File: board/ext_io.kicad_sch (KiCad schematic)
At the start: 34 parts, among them J13 AIN, J14 CAN_1, J15 DIO1, J16 DIO0, J17 CAN_2, SW10 Term, SW9 Term, U12 25LCxxx, U13 MCP2515-xP, U14 MCP3204, U15 MCP2562-E-P, U16 MCP2515-xP, U17 MCP23S17_SP, U18 MCP2562-E-P, Y2 16MHz, Y3 16MHz

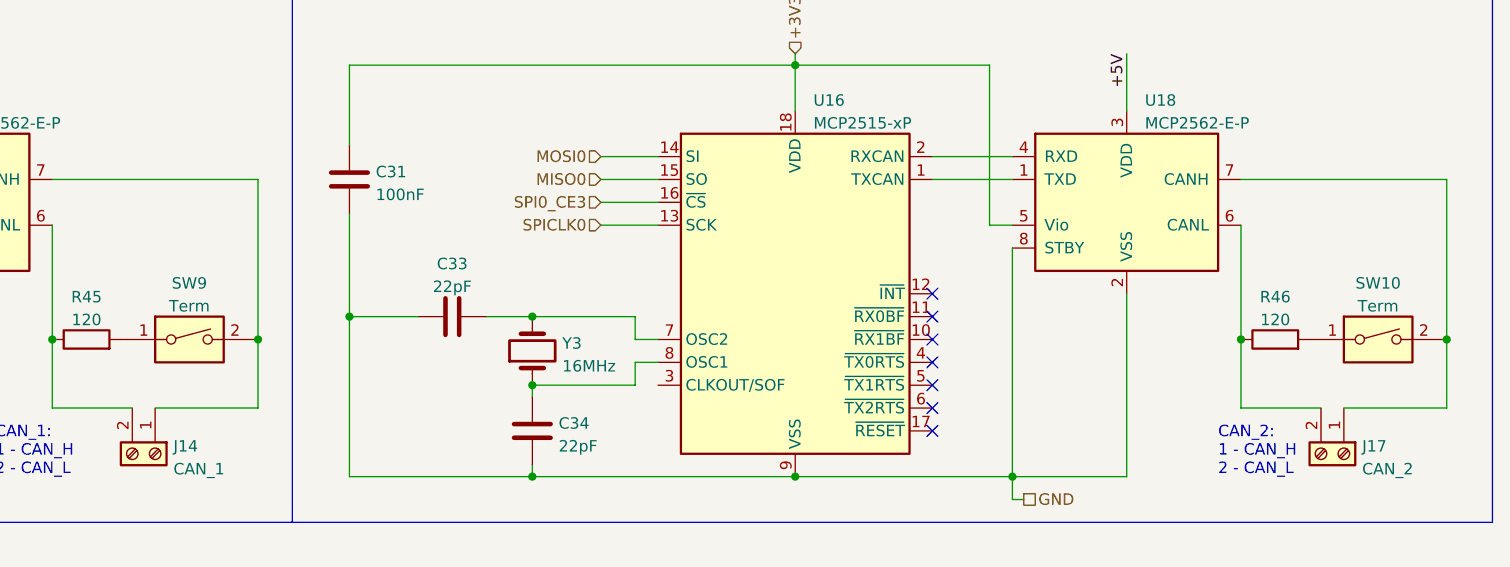
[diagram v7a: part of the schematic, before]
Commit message: Modularize board.
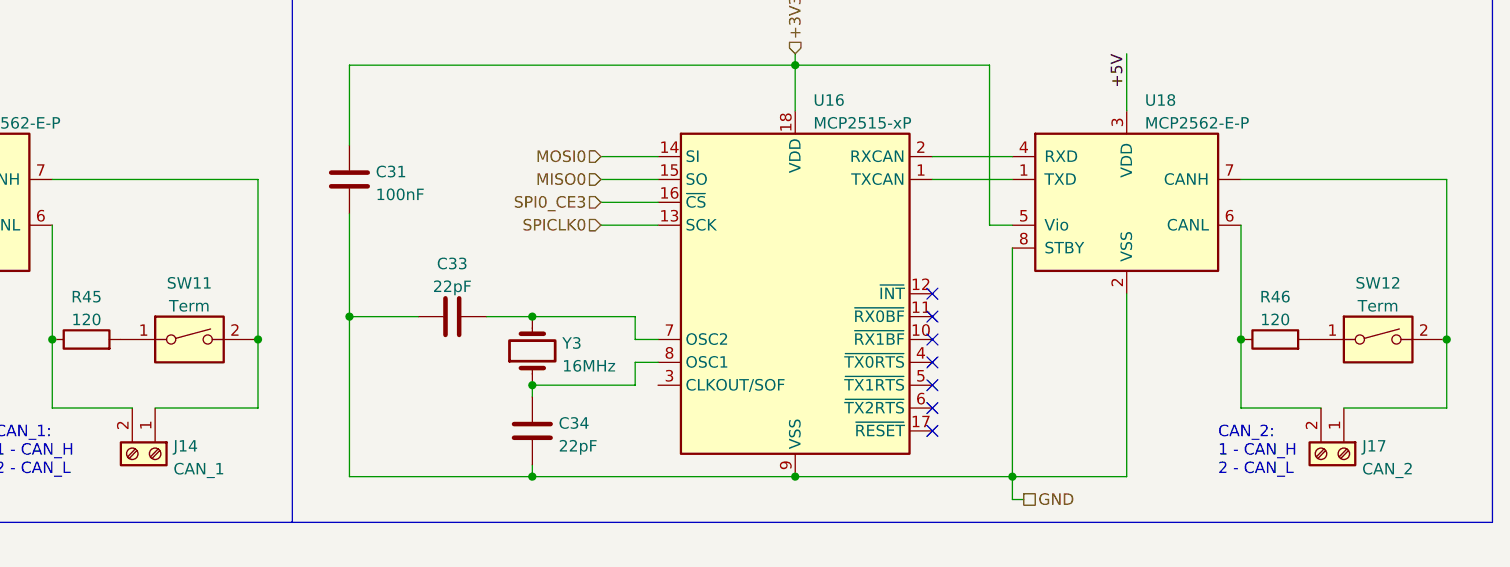
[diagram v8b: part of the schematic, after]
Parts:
- U14: footprint Package_DIP:DIP-12_W7.62mm_Socket_LongPads -> Package_DIP:DIP-14_W7.62mm_LongPads
- renumbered SW9 to SW11, SW10 to SW12
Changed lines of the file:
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@@
   (title_block
     (title "The Ulysses Board")
-    (date "2022-09-08")
+    (date "2022-09-15")
     (rev "1.3")
     (company "Dirk Gottschalk")
@@
   (symbol (lib_id "Switch:SW_DIP_x01") (at 133.35 142.24 0) (unit 1)
     (in_bom yes) (on_board yes) (fields_autoplaced)
-    (property "Reference" "SW9" (id 0) (at 133.35 136.0002 0))
+    (property "Reference" "SW11" (id 0) (at 133.35 136.0002 0))
     (property "Value" "Term" (id 1) (at 133.35 138.5371 0))
     (property "Footprint" "Button_Switch_THT:SW_DIP_SPSTx01_Slide_6.7x4.1mm_W7.62mm_P2.54mm_LowProfile" (id 2) (at 133.35 142.24 0)
@@
     (pin "1")
     (pin "2")
-  )
-  (symbol (lib_id "Analog_ADC:MCP3204") (at 96.52 55.88 0) (unit 1)
-    (in_bom yes) (on_board yes) (fields_autoplaced)
-    (property "Reference" "U14" (id 0) (at 98.5394 44.5602 0)
-      (effects (font (size 1.27 1.27)) (justify left))
-    )
-    (property "Value" "MCP3204" (id 1) (at 98.5394 47.0971 0)
-      (effects (font (size 1.27 1.27)) (justify left))
-    )
-    (property "Footprint" "Package_DIP:DIP-12_W7.62mm_Socket_LongPads" (id 2) (at 119.38 63.5 0)
-      (effects (font (size 1.27 1.27)) hide)
-    )
-    (property "Datasheet" "http://ww1.microchip.com/downloads/en/DeviceDoc/21298c.pdf" (id 3) (at 119.38 63.5 0)
-      (effects (font (size 1.27 1.27)) hide)
-    )
-    (pin "1")
-    (pin "10")
-    (pin "11")
-    (pin "12")
-    (pin "13")
-    (pin "14")
-    (pin "2")
-    (pin "3")
-    (pin "4")
-    (pin "5")
-    (pin "6")
-    (pin "7")
-    (pin "8")
-    (pin "9")
   )
   (symbol (lib_id "Device:C") (at 39.37 152.4 0) (unit 1)
@@
     (pin "2")
   )
+  (symbol (lib_id "Analog_ADC:MCP3204") (at 96.52 55.88 0) (unit 1)
+    (in_bom yes) (on_board yes) (fields_autoplaced)
+    (property "Reference" "U14" (id 0) (at 98.5394 44.5602 0)
+      (effects (font (size 1.27 1.27)) (justify left))
+    )
+    (property "Value" "MCP3204" (id 1) (at 98.5394 47.0971 0)
+      (effects (font (size 1.27 1.27)) (justify left))
+    )
+    (property "Footprint" "Package_DIP:DIP-14_W7.62mm_LongPads" (id 2) (at 119.38 63.5 0)
+      (effects (font (size 1.27 1.27)) hide)
+    )
+    (property "Datasheet" "http://ww1.microchip.com/downloads/en/DeviceDoc/21298c.pdf" (id 3) (at 119.38 63.5 0)
+      (effects (font (size 1.27 1.27)) hide)
+    )
+    (pin "1")
+    (pin "10")
+    (pin "11")
+    (pin "12")
+    (pin "13")
+    (pin "14")
+    (pin "2")
+    (pin "3")
+    (pin "4")
+    (pin "5")
+    (pin "6")
+    (pin "7")
+    (pin "8")
+    (pin "9")
+  )
   (symbol (lib_name "MCP2562-E-P_1") (lib_id "Interface_CAN_LIN_custom:MCP2562-E-P") (at 237.49 127 0) (unit 1)
     (in_bom yes) (on_board yes) (fields_autoplaced)
@@
   (symbol (lib_id "Switch:SW_DIP_x01") (at 265.43 142.24 0) (unit 1)
     (in_bom yes) (on_board yes) (fields_autoplaced)
-    (property "Reference" "SW10" (id 0) (at 265.43 136.0002 0))
+    (property "Reference" "SW12" (id 0) (at 265.43 136.0002 0))
     (property "Value" "Term" (id 1) (at 265.43 138.5371 0))
     (property "Footprint" "Button_Switch_THT:SW_DIP_SPSTx01_Slide_6.7x4.1mm_W7.62mm_P2.54mm_LowProfile" (id 2) (at 265.43 142.24 0)
